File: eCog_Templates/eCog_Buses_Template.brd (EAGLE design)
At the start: 47.5 x 28 mm, 3 parts

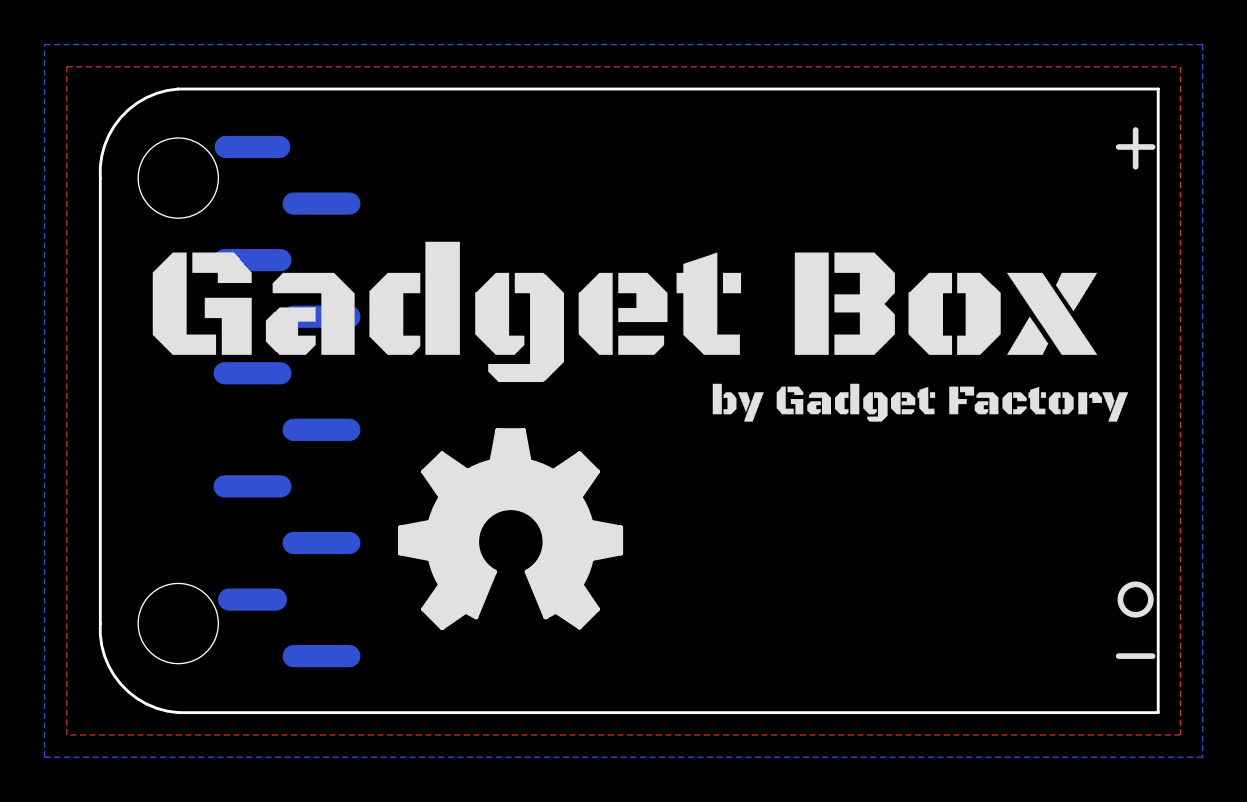
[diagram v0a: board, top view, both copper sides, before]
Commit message: Change to through hole and give bette descriptions.
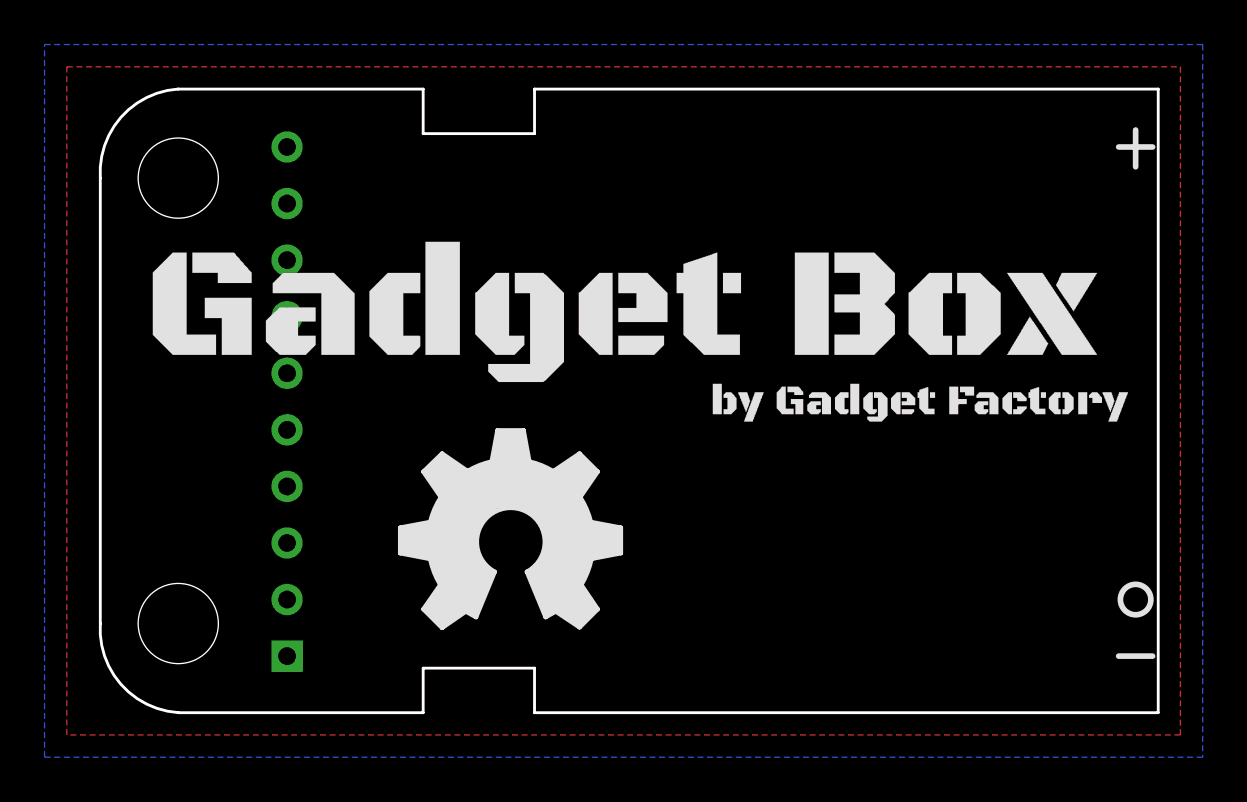
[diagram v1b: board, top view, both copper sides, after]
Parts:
- ECOG: value ECOG_BUSES_ROWECOG_BUSES_SMD -> ECOG_BUSES_ROWTHROUGHHOLE; device eCogs:ECOG_BUSES_SMD -> eCogs:ECOG_BUSES_TH
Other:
- outline, holes or cut-outs redrawn
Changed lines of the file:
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@@
 </autorouter>
 <elements>
-<element name="ECOG" library="eCogs" package="ECOG_BUSES_SMD" value="ECOG_BUSES_ROWECOG_BUSES_SMD" x="0" y="0" smashed="yes">
-<attribute name="DIGIKEY" value="S1013EC-10-ND" x="0" y="0" size="1.778" layer="27" display="off"/>
-</element>
+<element name="ECOG" library="eCogs" package="ECOG_BUSES_TH" value="ECOG_BUSES_ROWTHROUGHHOLE" x="0" y="0" smashed="yes"/>
 <element name="U$1" library="GadgetFactory" package="GADGETBOX_TEXT" value="" x="24.13" y="17.78"/>
 <element name="U$2" library="ohw-logo" package="OSHW_FILLX350_NOTEXT" value="" x="13.97" y="3.81"/>
